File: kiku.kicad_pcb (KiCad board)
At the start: 2 copper layers, 2 parts, among them U1 ESP32-S3-WROOM-1, U2 Value

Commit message: quite a bit of changes, still not finished with the schematic. havent committed in a while
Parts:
- added C2: 1 µF, Capacitor_SMD:C_0402_1005Metric, F.Cu at (194.1, 132.6)
- added C3: 1 µF, Capacitor_SMD:C_0603_1608Metric, F.Cu at (201.5, 78.3)
- added C4: 1 µF, Capacitor_SMD:C_0603_1608Metric, F.Cu at (201.5, 80.8)
- added C5: 1 µF, Capacitor_SMD:C_0603_1608Metric, F.Cu at (201.5, 83.3)
- added C6: 1 µF, Capacitor_SMD:C_0603_1608Metric, F.Cu at (201.5, 85.8)
- added C7: 1 µF, Capacitor_SMD:C_0603_1608Metric, F.Cu at (201.5, 88.3)
- added C8: 1 µF, Capacitor_SMD:C_0603_1608Metric, F.Cu at (201.5, 90.8)
- added C9: 10 µF, Capacitor_SMD:C_0603_1608Metric, F.Cu at (201.5, 93.3)
- added J1: BM02B-SRSS-TB LFSN, libraries:CONN_BM02B-SRSS-TB_JST, F.Cu at (148.8, 122.4)
- added J2: USB_C_Receptacle_USB2.0_16P, Connector_USB:USB_C_Receptacle_GCT_USB4105-xx-A_16P_TopMnt_Horizontal, F.Cu at (186.4, 112.5)
- added J3: Conn_Coaxial, Connector_Coaxial:SMA_Molex_73251-1153_EdgeMount_Horizontal, F.Cu at (132.6, 99.9)
- added R3: 2 kΩ, Resistor_SMD:R_0402_1005Metric, F.Cu at (186.3, 119.4)
- added R4: 5.1k, Resistor_SMD:R_0402_1005Metric, F.Cu at (186.3, 121.4)
- added R5: 5.1k, Resistor_SMD:R_0402_1005Metric, F.Cu at (186.3, 123.4)
- added R6: 10 kΩ, Resistor_SMD:R_0402_1005Metric, F.Cu at (186.3, 125.4)
- added R7: 10 kΩ, Resistor_SMD:R_0402_1005Metric, F.Cu at (186.3, 127.4)
- added R8: 390 kΩ, Resistor_SMD:R_0402_1005Metric, F.Cu at (186.3, 129.3)
- added R9: 100 kΩ, Resistor_SMD:R_0402_1005Metric, F.Cu at (186.3, 131.3)
- added SW1: SW_SPST, Button_Switch_SMD:SW_SPST_B3U-1100P, F.Cu at (206.4, 80.0)
- added SW2: SW_SPST, Button_Switch_SMD:SW_SPST_B3U-1100P, F.Cu at (206.4, 85.1)
- added TP1: TestPoint, TestPoint:TestPoint_Keystone_5010-5014_Multipurpose, F.Cu at (211.9, 79.5)
- added TP2: TestPoint, TestPoint:TestPoint_Keystone_5010-5014_Multipurpose, F.Cu at (211.9, 84.6)
- added U4: AMS1117-3.3, Package_TO_SOT_SMD:SOT-223-3_TabPin2, F.Cu at (134.9, 113.1)
- added U6: BQ25185DLHR, libraries:WSON10_DLH_TEX, F.Cu at (147.5, 82.5)
- U2: value Value -> Wio-sx1262-n
- moved U2 56.7 mm to (154.5, 101.8), turned to -90 degrees
- moved U1 39.8 mm to (166.2, 77.5)
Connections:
- U1 pad 1: Net-(U1-GND-Pad1) -> GND
- U1 pad 12: unconnected-(U1-IO8-Pad12) -> RESET
- U1 pad 15: unconnected-(U1-IO3-Pad15) -> MISO
- U1 pad 2: unconnected-(U1-3V3-Pad2) -> +3.3V
- U1 pad 27: unconnected-(U1-IO0-Pad27) -> BOOT
- U1 pad 3: unconnected-(U1-EN-Pad3) -> en
- U1 pad 39: unconnected-(U1-IO1-Pad39) -> BattVoltage
- U1 pad 40: Net-(U1-GND-Pad1) -> GND
- U1 pad 41: Net-(U1-GND-Pad1) -> GND
- U1 pad 5: unconnected-(U1-IO5-Pad5) -> SCK
- U1 pad 6: unconnected-(U1-IO6-Pad6) -> MOSI
- U1 pad 8: unconnected-(U1-IO15-Pad8) -> BUSY
- U1 pad 9: unconnected-(U1-IO16-Pad9) -> DIO1
- U2 pad 10: unconnected-(U2-GND2-Pad10) -> GND
- U2 pad 11: unconnected-(U2-BUSY-Pad11) -> BUSY
- U2 pad 12: unconnected-(U2-DIO1-Pad12) -> DIO1
- U2 pad 2: unconnected-(U2-MISO-Pad2) -> MISO
- U2 pad 3: unconnected-(U2-MOSI-Pad3) -> MOSI
- U2 pad 4: unconnected-(U2-SCK-Pad4) -> SCK
- U2 pad 5: unconnected-(U2-RST-Pad5) -> RESET
- U2 pad 6: unconnected-(U2-NSS-Pad6) -> NSS
- U2 pad 7: unconnected-(U2-GND1-Pad7) -> GND
- U2 pad 8: unconnected-(U2-VCC-Pad8) -> +3.3V
- U2 pad 9: unconnected-(U2-ANT-Pad9) -> ANT
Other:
- board outline added: 66.9 x 70 mm

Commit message: more work on the power stuff
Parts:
- added R10: 2.4 kΩ, Resistor_SMD:R_0402_1005Metric, F.Cu at (214.3, 95.5)
- added R11: 300Ω, Resistor_SMD:R_0402_1005Metric, F.Cu at (214.3, 97.5)
- added SW3: RESET CHARGER, Button_Switch_SMD:SW_SPST_B3U-1100P, F.Cu at (209.9, 97.5)
- SW1: value SW_SPST -> BOOT
- SW2: value SW_SPST -> EN
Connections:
- U6 pad 6: unconnected-(U6-TS/MR-Pad6) -> Net-(SW3-A)
- U6 pad 7: unconnected-(U6-ILIM/VSET-Pad7) -> Net-(U6-ILIM/VSET)
- U6 pad 8: unconnected-(U6-ISET-Pad8) -> Net-(U6-ISET)
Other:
- board text added: "kiku"

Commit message: mostly finished on the schematic, possibly starting on the routing
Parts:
- removed C2: 1 µF, Capacitor_SMD:C_0402_1005Metric
- removed R3: 2 kΩ, Resistor_SMD:R_0402_1005Metric
- added R12: 10 kΩ, Resistor_SMD:R_0402_1005Metric, F.Cu at (186.0, 135.5)
- moved R5 14.0 mm to (177.5, 112.5)
- moved R4 11.8 mm to (175.0, 118.0)
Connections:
- net BattVoltage renamed BATTVOLT
- U1 pad 38: unconnected-(U1-IO2-Pad38) -> CHGSWITCH
- U6 pad 4: unconnected-(U6-/CE-Pad4) -> CHGSWITCH
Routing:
- net GND: track 0.00 -> 76.6 mm
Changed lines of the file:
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@@
 			(size 1.5 0.9)
 			(layers "F.Cu" "F.Mask" "F.Paste")
-			(net "unconnected-(U1-IO2-Pad38)")
+			(net "CHGSWITCH")
 			(pinfunction "IO2_38")
 			(pintype "bidirectional")
@@
 			(size 1.5 0.9)
 			(layers "F.Cu" "F.Mask" "F.Paste")
-			(net "BattVoltage")
+			(net "BATTVOLT")
 			(pinfunction "IO1_39")
 			(pintype "bidirectional")
@@
 			(size 0.6604 0.2032)
 			(layers "F.Cu" "F.Mask" "F.Paste")
-			(net "unconnected-(U6-{slash}CE-Pad4)")
+			(net "CHGSWITCH")
 			(pinfunction "/CE_4")
 			(pintype "input")
@@
 	(footprint "Resistor_SMD:R_0402_1005Metric"
 		(layer "F.Cu")
-		(at 186.32 123.38)
+		(at 177.5 112.5)
 		(descr "Resistor SMD 0402 (1005 Metric), square (rectangular) end terminal, IPC-7351 nominal, (Body size source: IPC-SM-782 page 72, https://www.pcb-3d.com/wordpress/wp-content/uploads/ipc-sm-782a_amendment_1_and_2.pdf)")
 		(tags "resistor")
@@
 		)
 	)
-	(footprint "Resistor_SMD:R_0402_1005Metric"
-		(layer "F.Cu")
-		(at 186.32 119.4)
-		(descr "Resistor SMD 0402 (1005 Metric), square (rectangular) end terminal, IPC-7351 nominal, (Body size source: IPC-SM-782 page 72, https://www.pcb-3d.com/wordpress/wp-content/uploads/ipc-sm-782a_amendment_1_and_2.pdf)")
-		(tags "resistor")
-		(property "Reference" "R3"
-			(at 0 -1.17 0)
-			(layer "F.SilkS")
-			(effects
-				(font
-					(size 1 1)
-					(thickness 0.15)
-				)
-			)
-		)
-		(property "Value" "2 kΩ"
-			(at 0 1.17 0)
-			(layer "F.Fab")
-			(effects
-				(font
-					(size 1 1)
-					(thickness 0.15)
-				)
-			)
-		)
-		(property "Datasheet" ""
-			(at 0 0 0)
-			(layer "F.Fab")
-			(hide yes)
-			(effects
-				(font
-					(size 1.27 1.27)
-				)
-			)
-		)
-		(property "Description" "Resistor"
-			(at 0 0 0)
-			(layer "F.Fab")
-			(hide yes)
-			(effects
-				(font
-					(size 1.27 1.27)
-				)
-			)
-		)
-		(property "KiLib_Generator" "SMD_2terminal_chip_molded"
-			(at 0 0 0)
-			(layer "F.SilkS")
-			(hide yes)
-			(effects
-				(font
-					(size 1 1)
-					(thickness 0.15)
-				)
-			)
-		)
-		(property ki_fp_filters "R_*")
-		(sheetname "/")
-		(sheetfile "kiku.kicad_sch")
-		(units
-			(unit
-				(name "A")
-				(pins "1" "2")
-			)
-		)
-		(attr smd)
-		(duplicate_pad_numbers_are_jumpers no)
-		(fp_line
-			(start -0.153641 -0.38)
-			(end 0.153641 -0.38)
-			(stroke
-				(width 0.12)
-				(type solid)
-			)
-			(layer "F.SilkS")
-		)
-		(fp_line
-			(start -0.153641 0.38)
-			(end 0.153641 0.38)
-			(stroke
-				(width 0.12)
-				(type solid)
-			)
-			(layer "F.SilkS")
-		)
-		(fp_rect
-			(start -0.93 -0.47)
-			(end 0.93 0.47)
-			(stroke
-				(width 0.05)
-				(type solid)
-			)
-			(fill no)
-			(layer "F.CrtYd")
-		)
-		(fp_rect
-			(start -0.525 -0.27)
-			(end 0.525 0.27)
-			(stroke
-				(width 0.1)
-				(type solid)
-			)
-			(fill no)
-			(layer "F.Fab")
-		)
-		(fp_text user "${REFERENCE}"
-			(at 0 0 0)
-			(layer "F.Fab")
-			(effects
-				(font
-					(size 0.26 0.26)
-					(thickness 0.04)
-				)
-			)
-		)
-		(pad "1" smd roundrect
-			(at -0.51 0)
-			(size 0.54 0.64)
-			(layers "F.Cu" "F.Mask" "F.Paste")
-			(roundrect_rratio 0.25)
-			(net "Net-(U3-PROG)")
-			(pintype "passive")
-		)
-		(pad "2" smd roundrect
-			(at 0.51 0)
-			(size 0.54 0.64)
-			(layers "F.Cu" "F.Mask" "F.Paste")
-			(roundrect_rratio 0.25)
-			(net "GND")
-			(pintype "passive")
-		)
-		(embedded_fonts no)
-		(model "${KICAD10_3DMODEL_DIR}/Resistor_SMD.3dshapes/R_0402_1005Metric.stpZ"
-			(offset
-				(xyz 0 0 0)
-			)
-			(scale
-				(xyz 1 1 1)
-			)
-			(rotate
-				(xyz 0 0 0)
-			)
-		)
-	)
 	(footprint "libraries:Wio-SX1262 PCB Package"
 		(layer "F.Cu")
@@
 			(layers "F.Cu" "F.Mask" "F.Paste")
 			(roundrect_rratio 0.25)
-			(net "BattVoltage")
+			(net "BATTVOLT")
 			(pintype "passive")
 		)
@@
 			(layers "F.Cu" "F.Mask" "F.Paste")
 			(roundrect_rratio 0.25)
-			(net "BattVoltage")
+			(net "BATTVOLT")
 			(pintype "passive")
 		)
@@
 		)
 	)
-	(footprint "Capacitor_SMD:C_0402_1005Metric"
+	(footprint "Resistor_SMD:R_0402_1005Metric"
 		(layer "F.Cu")
-		(at 194.08 132.62)
-		(descr "Capacitor SMD 0402 (1005 Metric), square (rectangular) end terminal, IPC-7351 nominal, (Body size source: IPC-SM-782 page 76, https://www.pcb-3d.com/wordpress/wp-content/uploads/ipc-sm-782a_amendment_1_and_2.pdf)")
-		(tags "capacitor")
-		(property "Reference" "C2"
-			(at 0 -1.16 0)
+		(at 185.955 135.495)
+		(descr "Resistor SMD 0402 (1005 Metric), square (rectangular) end terminal, IPC-7351 nominal, (Body size source: IPC-SM-782 page 72, https://www.pcb-3d.com/wordpress/wp-content/uploads/ipc-sm-782a_amendment_1_and_2.pdf)")
+		(tags "resistor")
+		(property "Reference" "R12"
+			(at 0 -1.17 0)
 			(layer "F.SilkS")
 			(effects
@@
 			)
 		)
-		(property "Value" "1 µF"
-			(at 0 1.16 0)
+		(property "Value" "10 kΩ"
+			(at 0 1.17 0)
 			(layer "F.Fab")
 			(effects
@@
 			)
 		)
-		(property "Description" "Unpolarized capacitor"
+		(property "Description" "Resistor"
 			(at 0 0 0)
 			(layer "F.Fab")
@@
 			)
 		)
-		(property ki_fp_filters "C_*")
+		(property ki_fp_filters "R_*")
 		(sheetname "/")
 		(sheetfile "kiku.kicad_sch")
@@
 		(duplicate_pad_numbers_are_jumpers no)
 		(fp_line
-			(start -0.107836 -0.36)
-			(end 0.107836 -0.36)
+			(start -0.153641 -0.38)
+			(end 0.153641 -0.38)
 			(stroke
 				(width 0.12)
@@
 		)
 		(fp_line
-			(start -0.107836 0.36)
-			(end 0.107836 0.36)
+			(start -0.153641 0.38)
+			(end 0.153641 0.38)
 			(stroke
 				(width 0.12)
@@
 		)
 		(fp_rect
-			(start -0.91 -0.46)
-			(end 0.91 0.46)
+			(start -0.93 -0.47)
+			(end 0.93 0.47)
 			(stroke
 				(width 0.05)
@@
 		)
 		(fp_rect
-			(start -0.5 -0.25)
-			(end 0.5 0.25)
+			(start -0.525 -0.27)
+			(end 0.525 0.27)
 			(stroke
 				(width 0.1)
@@
 			(effects
 				(font
-					(size 0.25 0.25)
+					(size 0.26 0.26)
 					(thickness 0.04)
 				)
@@
 		)
 		(pad "1" smd roundrect
-			(at -0.48 0)
-			(size 0.56 0.62)
+			(at -0.51 0)
+			(size 0.54 0.64)
 			(layers "F.Cu" "F.Mask" "F.Paste")
 			(roundrect_rratio 0.25)
-			(net "GND")
+			(net "VBUS")
 			(pintype "passive")
 		)
 		(pad "2" smd roundrect
-			(at 0.48 0)
-			(size 0.56 0.62)
+			(at 0.51 0)
+			(size 0.54 0.64)
 			(layers "F.Cu" "F.Mask" "F.Paste")
 			(roundrect_rratio 0.25)
-			(net "VBUS")
+			(net "CHGSWITCH")
 			(pintype "passive")
 		)
 		(embedded_fonts no)
-		(model "${KICAD10_3DMODEL_DIR}/Capacitor_SMD.3dshapes/C_0402_1005Metric.stpZ"
+		(model "${KICAD10_3DMODEL_DIR}/Resistor_SMD.3dshapes/R_0402_1005Metric.stpZ"
 			(offset
 				(xyz 0 0 0)
@@
 	(footprint "Resistor_SMD:R_0402_1005Metric"
 		(layer "F.Cu")
-		(at 186.32 121.39)
+		(at 175 118)
 		(descr "Resistor SMD 0402 (1005 Metric), square (rectangular) end terminal, IPC-7351 nominal, (Body size source: IPC-SM-782 page 72, https://www.pcb-3d.com/wordpress/wp-content/uploads/ipc-sm-782a_amendment_1_and_2.pdf)")
 		(tags "resistor")
@@
 		)
 	)
+	(segment
+		(start 181.97 108.525)
+		(end 181.97 107.848629)
+		(width 0.2)
+		(layer "F.Cu")
+		(net "GND")
+	)
+	(segment
+		(start 189.4 78.368528)
+		(end 183.271472 72.24)
+		(width 0.2)
+		(layer "F.Cu")
+		(net "GND")
+	)
+	(segment
+		(start 189.4 100.418629)
+		(end 189.4 78.368528)
+		(width 0.2)
+		(layer "F.Cu")
+		(net "GND")
+	)
+	(segment
+		(start 183.271472 72.24)
+		(end 175 72.24)
+		(width 0.2)
+		(layer "F.Cu")
+		(net "GND")
+	)
+	(segment
+		(start 165 72.24)
+		(end 157.5 72.24)
+		(width 0.2)
+		(layer "F.Cu")
+		(net "GND")
+	)
+	(segment
+		(start 182.745 109.3)
+		(end 181.97 108.525)
+		(width 0.2)
+		(layer "F.Cu")
+		(net "GND")
+	)
+	(segment
+		(start 181.97 107.848629)
+		(end 189.4 100.418629)
+		(width 0.2)
+		(layer "F.Cu")
+		(net "GND")
+	)
+	(segment
+		(start 165 72.24)
+		(end 164.75 72.49)
+		(width 0.2)
+		(layer "F.Cu")
+		(net "GND")
+	)
+	(segment
+		(start 164.75 72.49)
+		(end 164.75 79.96)
+		(width 0.2)
+		(layer "F.Cu")
+		(net "GND")
+	)
+	(segment
+		(start 175 72.24)
+		(end 165 72.24)
+		(width 0.2)
+		(layer "F.Cu")
+		(net "GND")
+	)
 	(embedded_fonts no)

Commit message: think im mostly finished
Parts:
- added C10: 1 µF, Capacitor_SMD:C_0603_1608Metric, F.Cu at (173.5, 127.0)
- added C11: 1 µF, Capacitor_SMD:C_0603_1608Metric, F.Cu at (171.2, 127.0)
- added R13: 10 kΩ, Resistor_SMD:R_0402_1005Metric, F.Cu at (157.8, 79.6)
- added U5: AMS1117-3.3, Package_TO_SOT_SMD:SOT-223-3_TabPin2, F.Cu at (171.2, 120.2)
- TP1: value TestPoint -> PWR
- TP2: value TestPoint -> GND
- moved C3 71.5 mm to (143.5, 120.0), turned to 180 degrees
- moved C8 65.7 mm to (144.2, 123.0), turned to -90 degrees
- moved R10 64.3 mm to (159.0, 128.2), turned to 180 degrees
- moved R11 62.6 mm to (159.0, 126.8), turned to 180 degrees
- moved C4 61.3 mm to (157.2, 123.2)
- moved SW3 57.4 mm to (163.8, 131.7)
- moved R9 55.3 mm to (183.5, 76.1), turned to 45 degrees
- moved C9 54.3 mm to (157.2, 124.8)
- moved U6 45.4 mm to (153.5, 127.5)
- moved SW2 42.7 mm to (165.4, 96.8)
- moved C5 39.9 mm to (165.4, 100.2), turned to 180 degrees
- moved SW1 36.9 mm to (173.7, 96.8)
- moved R12 36.5 mm to (150.0, 129.2), turned to 90 degrees
- moved R8 36.0 mm to (150.5, 126.0), turned to 90 degrees
- moved R6 34.1 mm to (168.9, 96.1), turned to 180 degrees
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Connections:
- C3 pad 1: +3V3 -> +3.3V
- R12 pad 1: VBUS -> +3V3USB
- TP2 pad 1: unconnected-(TP2-Pad1) -> GND
- U1 pad 12: RESET -> MOSI
- U1 pad 5: SCK -> BUSY
- U1 pad 6: MOSI -> RESET
- U1 pad 8: BUSY -> SCK
- U4 pad 2: +3V3 -> +3.3V
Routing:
- net GND: track 76.6 -> 409.3 mm, vias 0 -> 3
- net CHGSWITCH: track 0.00 -> 90.4 mm, vias 0 -> 2
- net BATTVOLT: track 0.00 -> 81.2 mm
- net VBUS: track 0.00 -> 73.7 mm, vias 0 -> 2
- net +3.3V: track 0.00 -> 63.6 mm
- net BUSY: track 0.00 -> 46.4 mm
- net D-: track 0.00 -> 43.3 mm, vias 0 -> 2
- net D+: track 0.00 -> 42.2 mm, vias 0 -> 2
- net DIO1: track 0.00 -> 37.6 mm
- net ANT: track 0.00 -> 36.9 mm, vias 0 -> 2
- net +3V3USB: track 0.00 -> 35.2 mm, vias 0 -> 3
- net +BATT: track 0.00 -> 34.3 mm
- net RESET: track 0.00 -> 32.1 mm
- net en: track 0.00 -> 30.0 mm, vias 0 -> 2
- net SCK: track 0.00 -> 28.2 mm
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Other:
- board size 66.9 x 70 mm -> 58.8 x 59.6 mm
- board text added: "BOOT"
- board text added: "CHG RST"
- board text added: "GND"
- board text added: "PWR"
- board text added: "RST"
- board text added: "^ the board ends here"
- board text added: "dont even worry about the sharp corners, they dont exist"
- board text added: "maybe short circuits, idk"
- board text added: "the antenna is supposed to go there, trust me"

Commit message: wow i have a lot to do
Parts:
- removed C11, C3, C4, C6: 1 µF, Capacitor_SMD:C_0603_1608Metric
- removed R12: 10 kΩ, Resistor_SMD:R_0402_1005Metric
- removed U4, U5: AMS1117-3.3, Package_TO_SOT_SMD:SOT-223-3_TabPin2
- added D1: PZS52C3V9M1Q, Diode_SMD:D_0402_1005Metric, F.Cu at (202.8, 93.8)
- added D2: PZS52C3V9M1Q, Diode_SMD:D_0402_1005Metric, F.Cu at (202.8, 95.8)
- added L1: 1.5uH 70mOhm, Inductor_SMD:L_1008_2520Metric, F.Cu at (190.0, 129.0)
- added R14: 10 kΩ, Resistor_SMD:R_0402_1005Metric, F.Cu at (183.8, 139.3)
- added TP3: VSYS, libraries:smalltestpoint, F.Cu at (199.6, 91.8)
- added TP4: 3V3, libraries:smalltestpoint, F.Cu at (199.6, 94.9)
- added TP5: 3V3, libraries:smalltestpoint, F.Cu at (199.6, 97.9)
- added TP6: 3V3, libraries:smalltestpoint, F.Cu at (199.6, 101.0)
- added TP7: 3V3, libraries:smalltestpoint, F.Cu at (199.6, 104.0)
- added U3: TPS63001, Package_SON:Texas_DRC0010J_ThermalVias, F.Cu at (190.0, 133.3)
- C10: value 1 µF -> 47 µF
- R10: value 2.4 kΩ -> 13 kΩ
- TP1, TP2: footprint TestPoint:TestPoint_Keystone_5010-5014_Multipurpose -> libraries:smalltestpoint
- moved C10 46.2 mm to (203.2, 91.6), turned to 0 degrees
- moved U2 18.1 mm to (165.1, 117.5), turned to 90 degrees
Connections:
- C10 pad 1: VBUS -> +3V3
- C9 pad 1: +4.5V -> +VSYS
- R13 pad 1: +3.3V -> +3V3
- R8 pad 1: +BATT -> +VSYS
- U1 pad 2: +3.3V -> +3V3
- U1 pad 38: CHGSWITCH -> unconnected-(U1-IO2-Pad38)
- U2 pad 8: +3.3V -> +3V3
- U6 pad 1: +4.5V -> +VSYS
- U6 pad 4: CHGSWITCH -> GND
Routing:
- net GND: track 409.3 -> 0.00 mm, vias 3 -> 0
- net CHGSWITCH: track 90.4 -> 0.00 mm, vias 2 -> 0
- net BATTVOLT: track 81.2 -> 0.00 mm
- net VBUS: track 73.7 -> 0.00 mm, vias 2 -> 0
- net +3.3V: track 63.6 -> 0.00 mm
- net BUSY: track 46.4 -> 0.00 mm
- net D-: track 43.3 -> 0.00 mm, vias 2 -> 0
- net D+: track 42.2 -> 0.00 mm, vias 2 -> 0
- net DIO1: track 37.6 -> 0.00 mm
- net ANT: track 36.9 -> 0.00 mm, vias 2 -> 0
- net +3V3USB: track 35.2 -> 0.00 mm, vias 3 -> 0
- net +BATT: track 34.3 -> 0.00 mm
- net RESET: track 32.1 -> 0.00 mm
- net en: track 30.0 -> 0.00 mm, vias 2 -> 0
- net SCK: track 28.2 -> 0.00 mm
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- added copper zone on B.Cu, net GND
- added copper zone on F.Cu, net GND
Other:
- board text added: "VBUS"
- board text removed: "PWR"

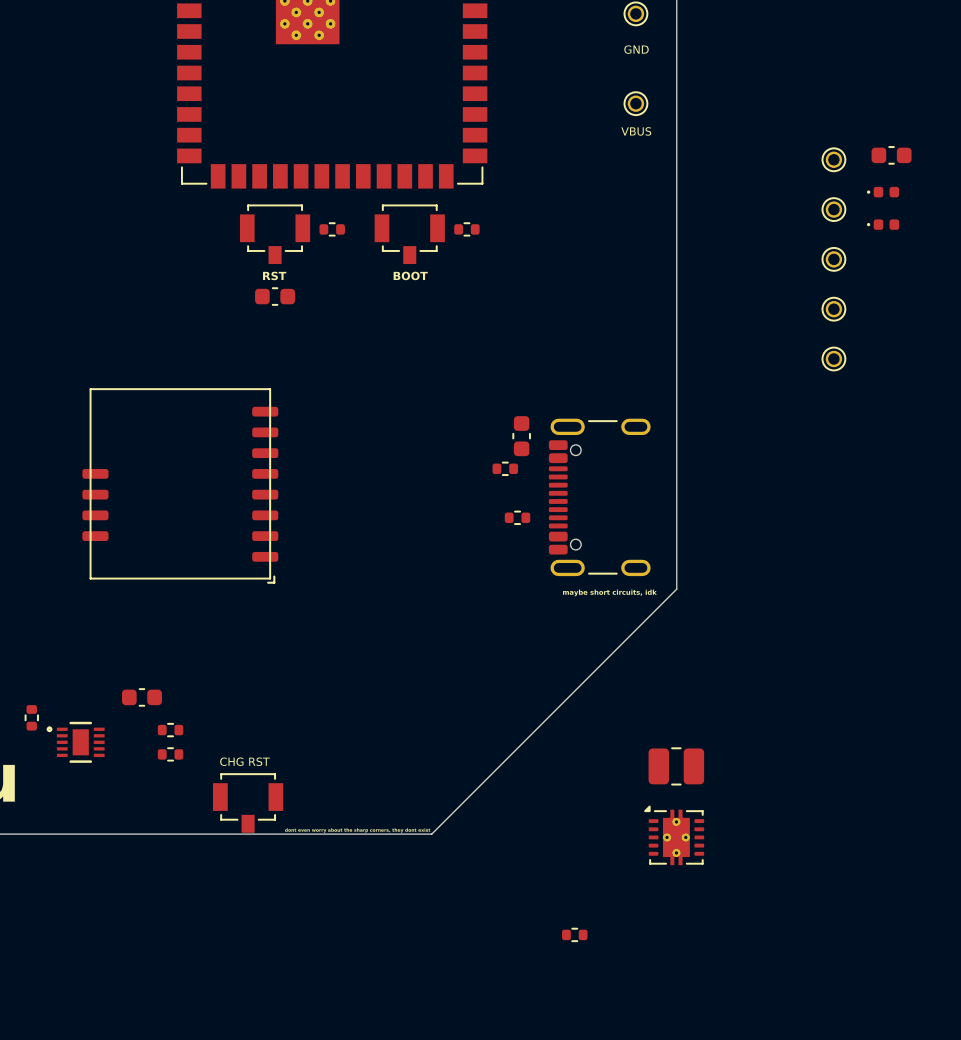
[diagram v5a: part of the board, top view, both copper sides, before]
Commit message: second attempt of routing
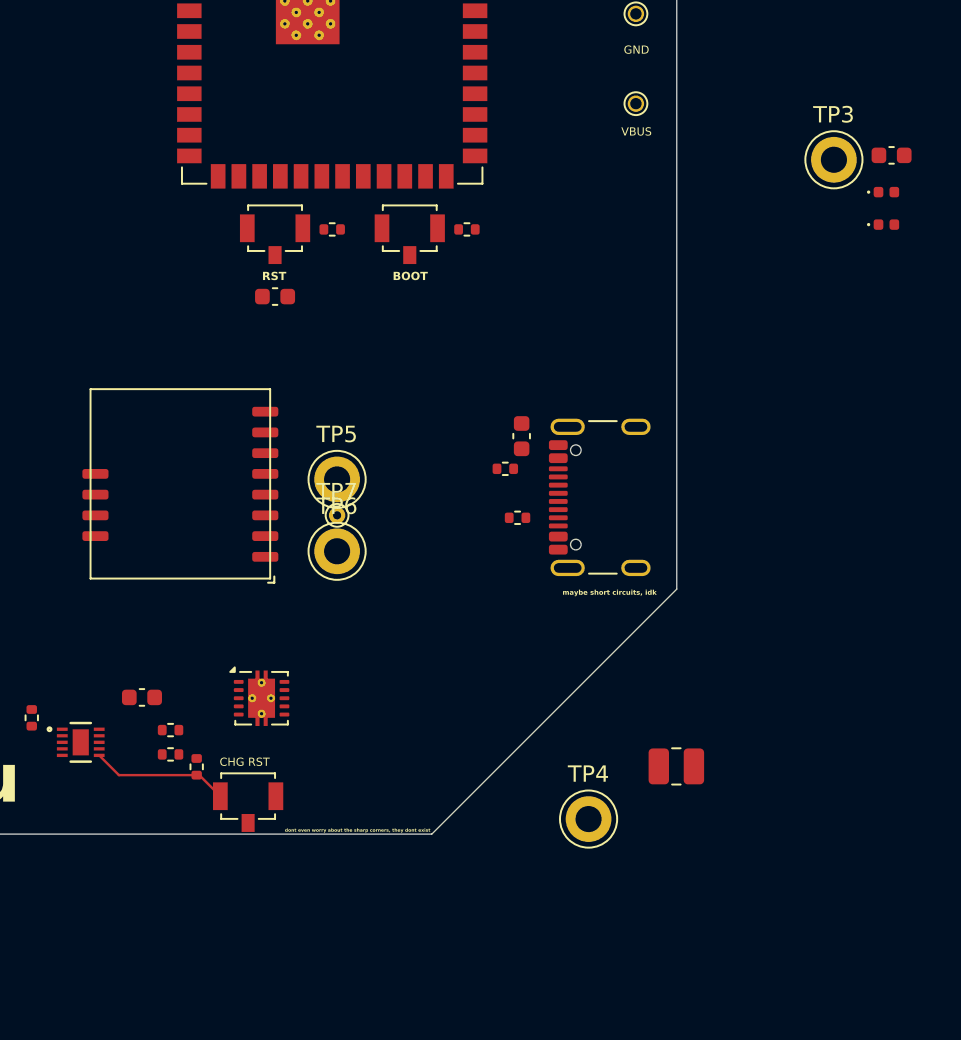
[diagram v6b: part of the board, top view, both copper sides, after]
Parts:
- TP3, TP4, TP5, TP6: footprint libraries:smalltestpoint -> TestPoint:TestPoint_Keystone_5010-5014_Multipurpose
- TP7: footprint libraries:smalltestpoint -> TestPoint:TestPoint_THTPad_D1.0mm_Drill0.5mm
- moved TP4 40.2 mm to (184.6, 132.2)
- moved TP6 33.8 mm to (169.2, 115.8)
- moved TP5 33.3 mm to (169.2, 111.4)
- moved TP7 31.9 mm to (169.2, 113.6)
- moved U3 26.8 mm to (164.6, 124.8)
- moved R14 25.3 mm to (160.6, 129.0), turned to 90 degrees
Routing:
- net Net-(SW3-A): track 0.00 -> 8.46 mm
